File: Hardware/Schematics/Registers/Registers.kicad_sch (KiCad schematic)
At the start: 19 parts, among them J1 Conn_01x19, J2 Conn_01x08, J3 Conn_01x08, U1 74LS139, U10 74LS245, U11 74LS245, U12 74LS245, U13 74LS245, U14 74LS245, U15 74LS245, U16 74LS245, U2 74LS139, U3 74LS377, U4 74LS377, U5 74LS377, U6 74LS377, U7 74LS377, U8 74LS377, U9 74LS245

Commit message: Interim
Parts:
- added D1, D10, D11, D12, D13, D14, D15, D16, D17, D18, D19, D2, D20, D21, D22, D23, D24, D25, D26, D27, D28, D29, D3, D30, D31, D32, D33, D34, D35, D36, D37, D38, D39, D4, D40, D41, D42, D43, D44, D45, D46, D47, D48, D5, D6, D7, D8, D9: LED, LED_THT:LED_D3.0mm, symbol Device:LED
- added RN1, RN2, RN3, RN4, RN5, RN6: R_Network08, Resistor_THT:R_Array_SIP9, symbol Device:R_Network08
- renumbered U4 to RD1, U6 to RS1
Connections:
- net GND: now also RN1.1 (common), RN2.1 (common), RN3.1 (common), RN4.1 (common), RN5.1 (common), RN6.1 (common)
- net VCC: now also U10.1 (A->B), U11.1 (A->B), U12.1 (A->B), U13.1 (A->B), U14.1 (A->B), U15.1 (A->B), U16.1 (A->B), U9.1 (A->B)
- net at U10.6 (A4), U3.12 (Q4), U9.6 (A4): now also D5.2 (A)
- net at U10.7 (A5), U3.15 (Q5), U9.7 (A5): now also D3.2 (A)
- net at U10.8 (A6), U3.16 (Q6), U9.8 (A6): now also D2.2 (A)
- net at U10.9 (A7), U3.19 (Q7), U9.9 (A7): now also D1.2 (A)
- net at U10.2 (A0), U3.2 (Q0), U9.2 (A0): now also D13.2 (A)
- net at U10.3 (A1), U3.5 (Q1), U9.3 (A1): now also D11.2 (A)
- net at U10.4 (A2), U3.6 (Q2), U9.4 (A2): now also D9.2 (A)
- net at U10.5 (A3), U3.9 (Q3), U9.5 (A3): now also D7.2 (A)
- net at U15.2 (A0), U16.2 (A0), U8.2 (Q0): now also D48.2 (A)
- net at U15.3 (A1), U16.3 (A1), U8.5 (Q1): now also D47.2 (A)
- net at U15.4 (A2), U16.4 (A2), U8.6 (Q2): now also D46.2 (A)
- net at U15.5 (A3), U16.5 (A3), U8.9 (Q3): now also D45.2 (A)
- net at U15.6 (A4), U16.6 (A4), U8.12 (Q4): now also D44.2 (A)
- net at U15.7 (A5), U16.7 (A5), U8.15 (Q5): now also D43.2 (A)
- net at U15.8 (A6), U16.8 (A6), U8.16 (Q6): now also D42.2 (A)
- net at U11.2 (A0), U12.2 (A0), U5.2 (Q0): now also D24.2 (A)
- net at U11.3 (A1), U12.3 (A1), U5.5 (Q1): now also D23.2 (A)
- net at U11.4 (A2), U12.4 (A2), U5.6 (Q2): now also D22.2 (A)
- net at U11.5 (A3), U12.5 (A3), U5.9 (Q3): now also D21.2 (A)
- net at U11.6 (A4), U12.6 (A4), U5.12 (Q4): now also D20.2 (A)
- net at U11.8 (A6), U12.8 (A6), U5.16 (Q6): now also D18.2 (A)
- net at U11.9 (A7), U12.9 (A7), U5.19 (Q7): now also D17.2 (A)
- net at J2.1 (Pin_1), RD1.2 (Q0): now also D16.2 (A)
- net at J2.2 (Pin_2), RD1.5 (Q1): now also D15.2 (A)
- net at J2.3 (Pin_3), RD1.6 (Q2): now also D14.2 (A)
- net at J2.4 (Pin_4), RD1.9 (Q3): now also D12.2 (A)
- net at J2.5 (Pin_5), RD1.12 (Q4): now also D10.2 (A)
- net at J2.6 (Pin_6), RD1.15 (Q5): now also D8.2 (A)
- net at J2.7 (Pin_7), RD1.16 (Q6): now also D6.2 (A)
- net at J2.8 (Pin_8), RD1.19 (Q7): now also D4.2 (A)
- net at U13.6 (A4), U14.6 (A4), U7.12 (Q4): now also D34.2 (A)
- net at U13.7 (A5), U14.7 (A5), U7.15 (Q5): now also D32.2 (A)
- net at U13.8 (A6), U14.8 (A6), U7.16 (Q6): now also D30.2 (A)
- net at U13.9 (A7), U14.9 (A7), U7.19 (Q7): now also D28.2 (A)
- net at U13.2 (A0), U14.2 (A0), U7.2 (Q0): now also D40.2 (A)
- net at U13.3 (A1), U14.3 (A1), U7.5 (Q1): now also D39.2 (A)
- net at U13.4 (A2), U14.4 (A2), U7.6 (Q2): now also D38.2 (A)
- net at U13.5 (A3), U14.5 (A3), U7.9 (Q3): now also D36.2 (A)
- net at J3.1 (Pin_1), RS1.2 (Q0): now also D37.2 (A)
- net at J3.2 (Pin_2), RS1.5 (Q1): now also D35.2 (A)
- net at J3.3 (Pin_3), RS1.6 (Q2): now also D33.2 (A)
- net at J3.4 (Pin_4), RS1.9 (Q3): now also D31.2 (A)
- net at J3.5 (Pin_5), RS1.12 (Q4): now also D29.2 (A)
- net at J3.6 (Pin_6), RS1.15 (Q5): now also D27.2 (A)
- net at J3.7 (Pin_7), RS1.16 (Q6): now also D26.2 (A)
- net at J3.8 (Pin_8), RS1.19 (Q7): now also D25.2 (A)
- net at U5.15 (Q5): now also D19.2 (A)
- net at U8.19 (Q7): now also D41.2 (A)
- new net: D47.1 (K), RN6.3 (R2)
- new net: D46.1 (K), RN6.4 (R3)
- new net: D45.1 (K), RN6.5 (R4)
- new net: D39.1 (K), RN5.3 (R2)
- new net: D5.1 (K), RN1.6 (R5)
- new net: D24.1 (K), RN3.2 (R1)
- new net: D23.1 (K), RN3.3 (R2)
- new net: D22.1 (K), RN3.4 (R3)
- new net: D21.1 (K), RN3.5 (R4)
- new net: D20.1 (K), RN3.6 (R5)
- new net: D19.1 (K), RN3.7 (R6)
- new net: D18.1 (K), RN3.8 (R7)
- new net: D17.1 (K), RN3.9 (R8)
- new net: D1.1 (K), RN1.9 (R8)
- new net: D43.1 (K), RN6.7 (R6)
- new net: D32.1 (K), RN5.7 (R6)
- new net: D8.1 (K), RN2.7 (R6)
- new net: D48.1 (K), RN6.2 (R1)
- new net: D16.1 (K), RN2.2 (R1)
- new net: D15.1 (K), RN2.3 (R2)
- new net: D14.1 (K), RN2.4 (R3)
- new net: D12.1 (K), RN2.5 (R4)
- new net: D10.1 (K), RN2.6 (R5)
- new net: D6.1 (K), RN2.8 (R7)
- new net: D4.1 (K), RN2.9 (R8)
- new net: D28.1 (K), RN5.9 (R8)
- new net: D13.1 (K), RN1.2 (R1)
- new net: D29.1 (K), RN4.6 (R5)
- new net: D2.1 (K), RN1.8 (R7)
- new net: D7.1 (K), RN1.5 (R4)
- new net: D11.1 (K), RN1.3 (R2)
- new net: D9.1 (K), RN1.4 (R3)
- new net: D3.1 (K), RN1.7 (R6)
- new net: D25.1 (K), RN4.9 (R8)
- new net: D34.1 (K), RN5.6 (R5)
- new net: D37.1 (K), RN4.2 (R1)
- new net: D35.1 (K), RN4.3 (R2)
- new net: D33.1 (K), RN4.4 (R3)
- new net: D31.1 (K), RN4.5 (R4)
- new net: D27.1 (K), RN4.7 (R6)
- new net: D26.1 (K), RN4.8 (R7)
- new net: D41.1 (K), RN6.9 (R8)
- new net: D42.1 (K), RN6.8 (R7)
- new net: D40.1 (K), RN5.2 (R1)
- new net: D38.1 (K), RN5.4 (R3)
- new net: D36.1 (K), RN5.5 (R4)
- new net: D30.1 (K), RN5.8 (R7)
- new net: D44.1 (K), RN6.6 (R5)
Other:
- moved on the sheet: J2, J3

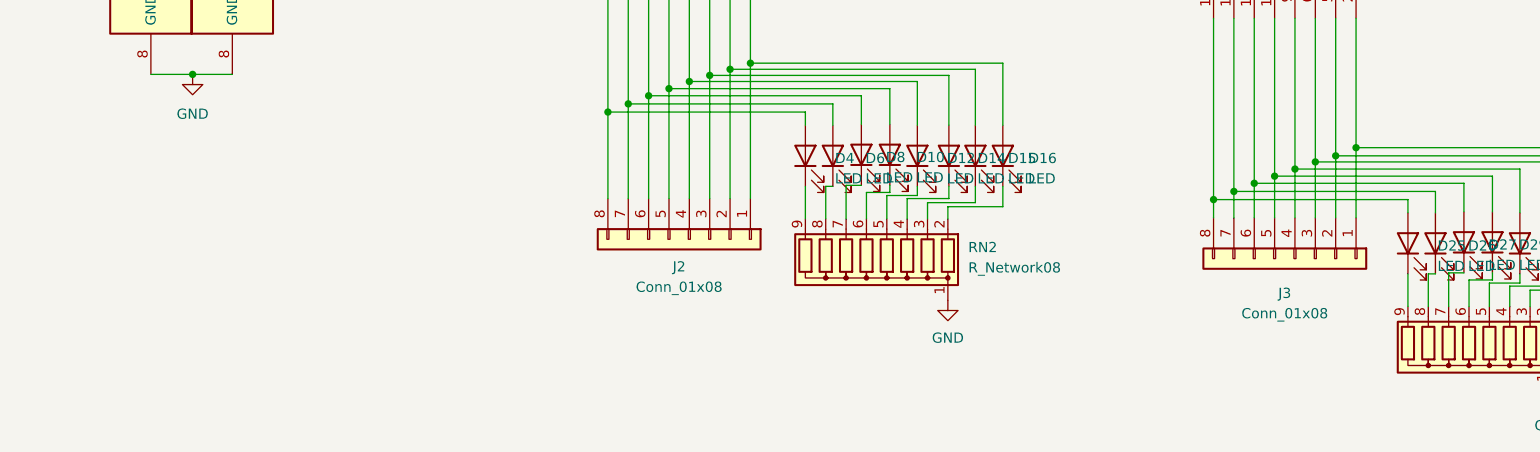
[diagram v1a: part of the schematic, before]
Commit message: Added Datapath Controller
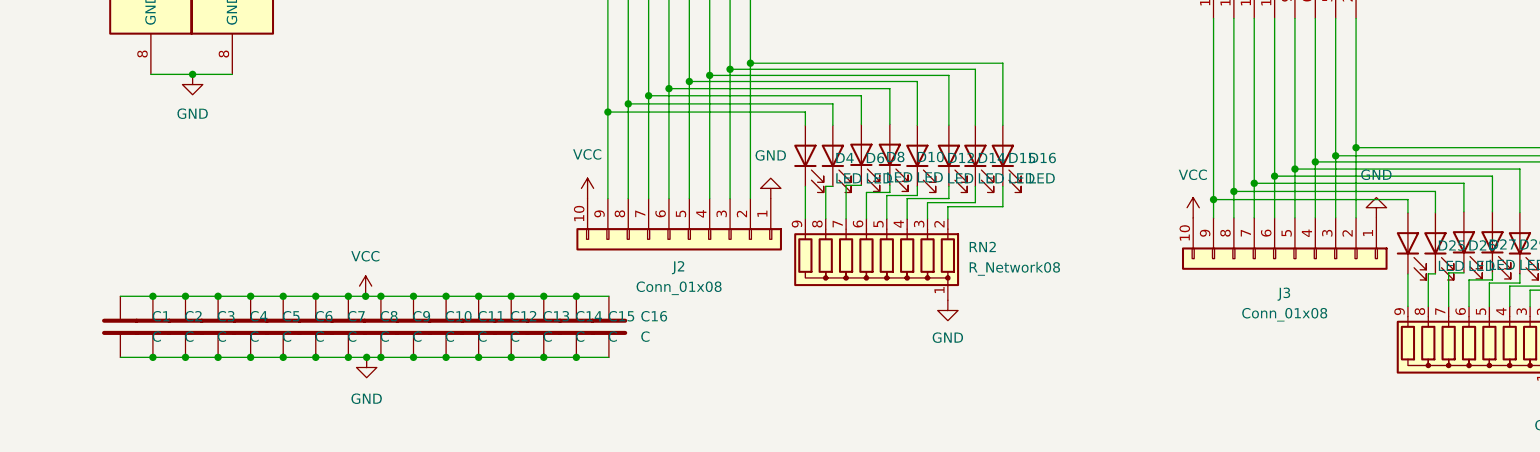
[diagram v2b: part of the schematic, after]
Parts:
- added C1, C10, C11, C12, C13, C14, C15, C16, C2, C3, C4, C5, C6, C7, C8, C9: C, Capacitor_THT:C_Rect_L9.0mm_W2.5mm_P7.50mm_MKT, symbol Device:C
- J2, J3: symbol Connector_Generic:Conn_01x08 -> Connector_Generic:Conn_01x10
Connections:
- net GND: now also J2.1 (Pin_1), J3.1 (Pin_1), C1.2, C10.2, C11.2, C12.2, C13.2, C14.2, C15.2, C16.2, C2.2, C3.2, C4.2, C5.2, C6.2, C7.2, C8.2, C9.2
- net VCC: now also J2.10 (Pin_10), J3.10 (Pin_10), C1.1, C10.1, C11.1, C12.1, C13.1, C14.1, C15.1, C16.1, C2.1, C3.1, C4.1, C5.1, C6.1, C7.1, C8.1, C9.1
- net at D8.2 (A), RD1.15 (Q5): now also J2.7 (Pin_7); no longer J2.6 (Pin_6)
- net at D16.2 (A), RD1.2 (Q0): now also J2.2 (Pin_2); no longer J2.1 (Pin_1)
- net at D15.2 (A), RD1.5 (Q1): now also J2.3 (Pin_3); no longer J2.2 (Pin_2)
- net at D14.2 (A), RD1.6 (Q2): now also J2.4 (Pin_4); no longer J2.3 (Pin_3)
- net at D12.2 (A), RD1.9 (Q3): now also J2.5 (Pin_5); no longer J2.4 (Pin_4)
- net at D10.2 (A), RD1.12 (Q4): now also J2.6 (Pin_6); no longer J2.5 (Pin_5)
- net at D6.2 (A), RD1.16 (Q6): now also J2.8 (Pin_8); no longer J2.7 (Pin_7)
- net at D4.2 (A), RD1.19 (Q7): now also J2.9 (Pin_9); no longer J2.8 (Pin_8)
- net at D29.2 (A), RS1.12 (Q4): now also J3.6 (Pin_6); no longer J3.5 (Pin_5)
- net at D37.2 (A), RS1.2 (Q0): now also J3.2 (Pin_2); no longer J3.1 (Pin_1)
- net at D35.2 (A), RS1.5 (Q1): now also J3.3 (Pin_3); no longer J3.2 (Pin_2)
- net at D33.2 (A), RS1.6 (Q2): now also J3.4 (Pin_4); no longer J3.3 (Pin_3)
- net at D31.2 (A), RS1.9 (Q3): now also J3.5 (Pin_5); no longer J3.4 (Pin_4)
- net at D27.2 (A), RS1.15 (Q5): now also J3.7 (Pin_7); no longer J3.6 (Pin_6)
- net at D26.2 (A), RS1.16 (Q6): now also J3.8 (Pin_8); no longer J3.7 (Pin_7)
- net at D25.2 (A), RS1.19 (Q7): now also J3.9 (Pin_9); no longer J3.8 (Pin_8)

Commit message: Finished Datapath Controller
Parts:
- J2, J3: footprint Connector_PinHeader_2.54mm:PinHeader_1x08_P2.54mm_Vertical -> Connector_PinHeader_2.54mm:PinHeader_1x10_P2.54mm_Vertical
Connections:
- net at U3.18 (D7), U5.18 (D7), U7.18 (D7)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: now also J1.10 (Pin_10)
- net at U3.3 (D0), U5.3 (D0), U7.3 (D0)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: now also J1.3 (Pin_3)
- net at U15.13 (B5): now also RD1.14 (D5), U11.13 (B5), U13.13 (B5), U9.13 (B5)
- net at U15.9 (A7), U16.9 (A7): now also D41.2 (A), U8.19 (Q7)
- net at U11.7 (A5), U12.7 (A5): now also D19.2 (A), U5.15 (Q5)

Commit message: Updated Schematics
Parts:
- removed C1, C10, C11, C12, C13, C14, C15, C16, C2, C3, C4, C5, C6, C7, C8, C9: C, Capacitor_THT:C_Rect_L9.0mm_W2.5mm_P7.50mm_MKT, symbol Device:C
- removed D1, D10, D11, D12, D13, D14, D15, D16, D17, D18, D19, D2, D20, D21, D22, D23, D24, D25, D26, D27, D28, D29, D3, D30, D31, D32, D33, D34, D35, D36, D37, D38, D39, D4, D40, D41, D42, D43, D44, D45, D46, D47, D48, D5, D6, D7, D8, D9: LED, LED_THT:LED_D3.0mm, symbol Device:LED
- removed J1: Conn_01x19, Connector_PinHeader_2.54mm:PinHeader_1x19_P2.54mm_Vertical, symbol Connector_Generic:Conn_01x19
- removed J3: Conn_01x08, Connector_PinHeader_2.54mm:PinHeader_1x10_P2.54mm_Vertical, symbol Connector_Generic:Conn_01x10
- removed RD1, RS1, U5, U7, U8: 74LS377, Package_DIP:DIP-20_W7.62mm_LongPads, symbol 74xx:74LS377
- removed RN1, RN2, RN3, RN4, RN5, RN6: R_Network08, Resistor_THT:R_Array_SIP9, symbol Device:R_Network08
- removed U10, U11, U12, U13, U14, U15, U16, U9: 74LS245, Package_DIP:DIP-20_W7.62mm_LongPads, symbol 74xx:74LS245
- removed unit 2 of U2
- added J1: Conn_02x05_Counter_Clockwise, Connector_PinHeader_2.54mm:PinHeader_2x05_P2.54mm_Vertical, symbol Connector_Generic:Conn_02x05_Counter_Clockwise
- added J3, J4, J5, J6: Conn_02x15_Counter_Clockwise, Connector_PinHeader_2.54mm:PinHeader_2x15_P2.54mm_Vertical, symbol Connector_Generic:Conn_02x15_Odd_Even
- added J7, J8: Conn_01x10, Connector_PinHeader_2.54mm:PinHeader_1x10_P2.54mm_Vertical, symbol Connector_Generic:Conn_01x10
- added U4: 74LS377, Package_DIP:DIP-20_W7.62mm_Socket_LongPads, symbol 74xx:74LS377
- J2: value Conn_01x08 -> Conn_01x10
- U1, U2: footprint Package_DIP:DIP-16_W7.62mm_LongPads -> Package_DIP:DIP-16_W7.62mm_Socket_LongPads
- U3: footprint Package_DIP:DIP-20_W7.62mm_LongPads -> Package_DIP:DIP-20_W7.62mm_Socket_LongPads
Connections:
- net GND: now also J1.6 (Pin_6), J3.30 (Pin_30), J4.30 (Pin_30), J5.30 (Pin_30), J6.30 (Pin_30), J7.10 (Pin_10), J8.10 (Pin_10), U4.10 (GND)
- net RS_{0}: now also J3.18 (Pin_18), J4.18 (Pin_18), J5.18 (Pin_18), J6.18 (Pin_18), U4.3 (D0)
- net RS_{1}: now also J3.20 (Pin_20), J4.20 (Pin_20), J5.20 (Pin_20), J6.20 (Pin_20), U4.4 (D1)
- net RS_{2}: now also J3.22 (Pin_22), J4.22 (Pin_22), J5.22 (Pin_22), J6.22 (Pin_22), U4.7 (D2)
- net RS_{3}: now also J3.24 (Pin_24), J4.24 (Pin_24), J5.24 (Pin_24), J6.24 (Pin_24), U4.8 (D3)
- net RS_{4}: now also J3.26 (Pin_26), J4.26 (Pin_26), J5.26 (Pin_26), J6.26 (Pin_26), U4.13 (D4)
- net RS_{5}: now also J3.28 (Pin_28), J4.28 (Pin_28), J5.28 (Pin_28), J6.28 (Pin_28), U4.14 (D5)
- net RS_{6}: now also J3.29 (Pin_29), J4.29 (Pin_29), J5.29 (Pin_29), J6.29 (Pin_29), U4.17 (D6)
- net RS_{7}: now also J3.27 (Pin_27), J4.27 (Pin_27), J5.27 (Pin_27), J6.27 (Pin_27), U4.18 (D7)
- net VCC: now also J1.1 (Pin_1), J3.1 (Pin_1), J4.1 (Pin_1), J5.1 (Pin_1), J6.1 (Pin_1), J7.1 (Pin_1), J8.1 (Pin_1), U4.20 (VCC)
- net at U2.4 (O0): now also J3.25 (Pin_25); no longer U3.1 (~{E})
- net CLK: now reaches U3.11 (CP)
- net CLK: now also J1.5 (Pin_5), J3.19 (Pin_19), J4.19 (Pin_19), J5.19 (Pin_19), J6.19 (Pin_19), U4.11 (CP)
- net at U3.12 (Q4): now also J7.6 (Pin_6)
- net RD_{4}: now reaches U3.13 (D4)
- net RD_{4}: now also J3.10 (Pin_10), J4.10 (Pin_10), J5.10 (Pin_10), J6.10 (Pin_10)
- net RD_{5}: now reaches U3.14 (D5)
- net RD_{5}: now also J3.12 (Pin_12), J4.12 (Pin_12), J5.12 (Pin_12), J6.12 (Pin_12)
- net at U3.15 (Q5): now also J7.7 (Pin_7)
- net at U3.16 (Q6): now also J7.8 (Pin_8)
- net RD_{6}: now reaches U3.17 (D6)
- net RD_{6}: now also J3.14 (Pin_14), J4.14 (Pin_14), J5.14 (Pin_14), J6.14 (Pin_14)
- net RD_{7}: now reaches U3.18 (D7)
- net RD_{7}: now also J3.16 (Pin_16), J4.16 (Pin_16), J5.16 (Pin_16), J6.16 (Pin_16)
- net at U3.19 (Q7): now also J7.9 (Pin_9)
- net at U3.2 (Q0): now also J7.2 (Pin_2)
- net RD_{0}: now reaches U3.3 (D0)
- net RD_{0}: now also J3.2 (Pin_2), J4.2 (Pin_2), J5.2 (Pin_2), J6.2 (Pin_2)
- net RD_{1}: now reaches U3.4 (D1)
- net RD_{1}: now also J3.4 (Pin_4), J4.4 (Pin_4), J5.4 (Pin_4), J6.4 (Pin_4)
- net at U3.5 (Q1): now also J7.3 (Pin_3)
- net at U3.6 (Q2): now also J7.4 (Pin_4)
- net RD_{2}: now reaches U3.7 (D2)
- net RD_{2}: now also J3.6 (Pin_6), J4.6 (Pin_6), J5.6 (Pin_6), J6.6 (Pin_6)
- net RD_{3}: now reaches U3.8 (D3)
- net RD_{3}: now also J3.8 (Pin_8), J4.8 (Pin_8), J5.8 (Pin_8), J6.8 (Pin_8)
- net at U3.9 (Q3): now also J7.5 (Pin_5)
- net D_{2}: now reaches J2.7 (Pin_7)
- net D_{2}: now also J3.7 (Pin_7), J4.7 (Pin_7), J5.7 (Pin_7), J6.7 (Pin_7)
- net D_{7}: now reaches J2.2 (Pin_2)
- net D_{7}: now also J3.17 (Pin_17), J4.17 (Pin_17), J5.17 (Pin_17), J6.17 (Pin_17)
- net D_{6}: now reaches J2.3 (Pin_3)
- net D_{6}: now also J3.15 (Pin_15), J4.15 (Pin_15), J5.15 (Pin_15), J6.15 (Pin_15)
- net D_{5}: now reaches J2.4 (Pin_4)
- net D_{5}: now also J3.13 (Pin_13), J4.13 (Pin_13), J5.13 (Pin_13), J6.13 (Pin_13)
- net D_{4}: now reaches J2.5 (Pin_5)
- net D_{4}: now also J3.11 (Pin_11), J4.11 (Pin_11), J5.11 (Pin_11), J6.11 (Pin_11)
- net D_{3}: now reaches J2.6 (Pin_6)
- net D_{3}: now also J3.9 (Pin_9), J4.9 (Pin_9), J5.9 (Pin_9), J6.9 (Pin_9)
- net D_{1}: now reaches J2.8 (Pin_8)
- net D_{1}: now also J3.5 (Pin_5), J4.5 (Pin_5), J5.5 (Pin_5), J6.5 (Pin_5)
- net D_{0}: now reaches J2.9 (Pin_9)
- net D_{0}: now also J3.3 (Pin_3), J4.3 (Pin_3), J5.3 (Pin_3), J6.3 (Pin_3)
- net at U2.6 (O2): now also J5.25 (Pin_25)
- net at U1.3 (A1): now also U1.13 (A1), J1.10 (Pin_10)
- net at U1.2 (A0): now also U1.14 (A0), J1.9 (Pin_9)
- net at U1.1 (E): now also J1.2 (Pin_2)
- net at U1.15 (E): now also U3.1 (~{E}), J1.3 (Pin_3)
- net at U2.3 (A1): now also J1.8 (Pin_8)
- net at U2.2 (A0): now also J1.7 (Pin_7)
- net at U2.1 (E): now also J1.4 (Pin_4)
- net at U2.5 (O1): now also J4.25 (Pin_25)
- net at U2.7 (O3): now also J6.25 (Pin_25)
- net RD_{SelectA}: no longer names the net of U1.12 (O0)
- net RD_{SelectA}: now also J3.23 (Pin_23)
- net RD_{SelectB}: no longer names the net of U1.11 (O1)
- net RD_{SelectB}: now also J4.23 (Pin_23)
- net RD_{SelectX}: no longer names the net of U1.10 (O2)
- net RD_{SelectX}: now also J5.23 (Pin_23)
- net RD_{SelectY}: no longer names the net of U1.9 (O3)
- net RD_{SelectY}: now also J6.23 (Pin_23)
- net RS_{SelectA}: no longer names the net of U1.4 (O0)
- net RS_{SelectA}: now also J3.21 (Pin_21)
- net RS_{SelectB}: no longer names the net of U1.5 (O1)
- net RS_{SelectB}: now also J4.21 (Pin_21)
- net RS_{SelectX}: no longer names the net of U1.6 (O2)
- net RS_{SelectX}: now also J5.21 (Pin_21)
- net RS_{SelectY}: no longer names the net of U1.7 (O3)
- net RS_{SelectY}: now also J6.21 (Pin_21)
- new net: J8.6 (Pin_6), U4.12 (Q4)
- new net: J8.7 (Pin_7), U4.15 (Q5)
- new net: J8.8 (Pin_8), U4.16 (Q6)
- new net: J8.9 (Pin_9), U4.19 (Q7)
- new net: J8.2 (Pin_2), U4.2 (Q0)
- new net: J8.3 (Pin_3), U4.5 (Q1)
- new net: J8.4 (Pin_4), U4.6 (Q2)
- new net: J8.5 (Pin_5), U4.9 (Q3)
